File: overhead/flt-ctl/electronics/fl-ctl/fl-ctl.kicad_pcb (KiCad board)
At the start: 2 copper layers, 145 x 47.3 mm, 31 parts, among them J1 Conn_02x01, J2 Conn_02x05_Counter_Clockwise

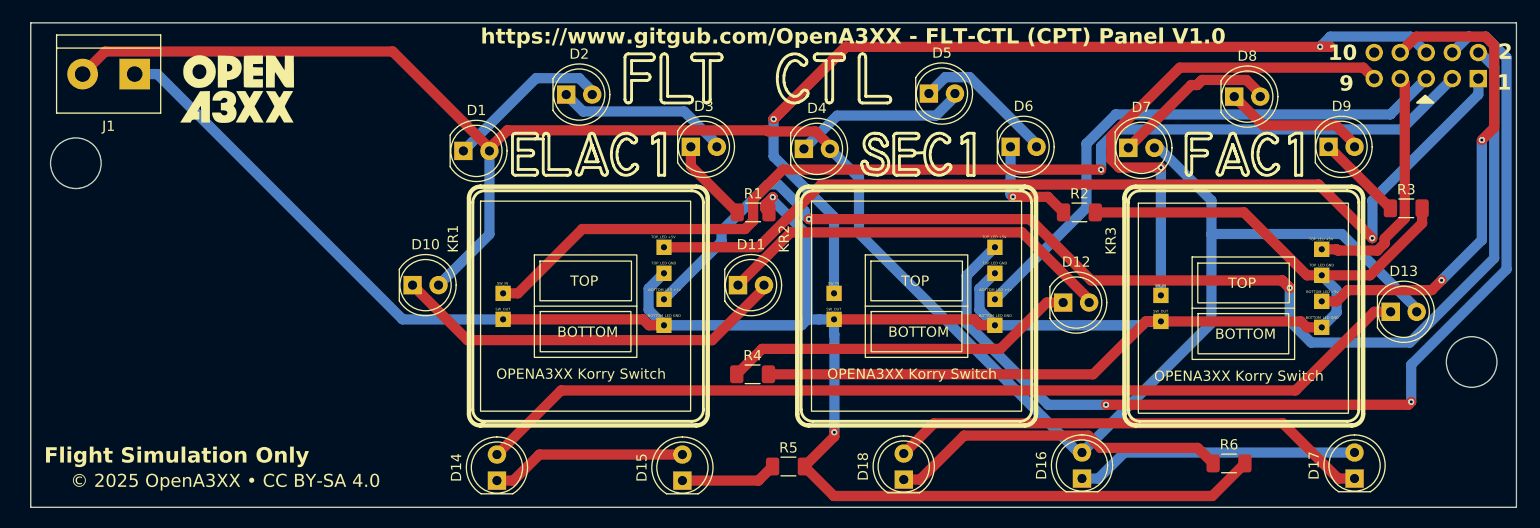
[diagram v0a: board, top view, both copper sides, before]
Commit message: Updated all LEDs for SMD!
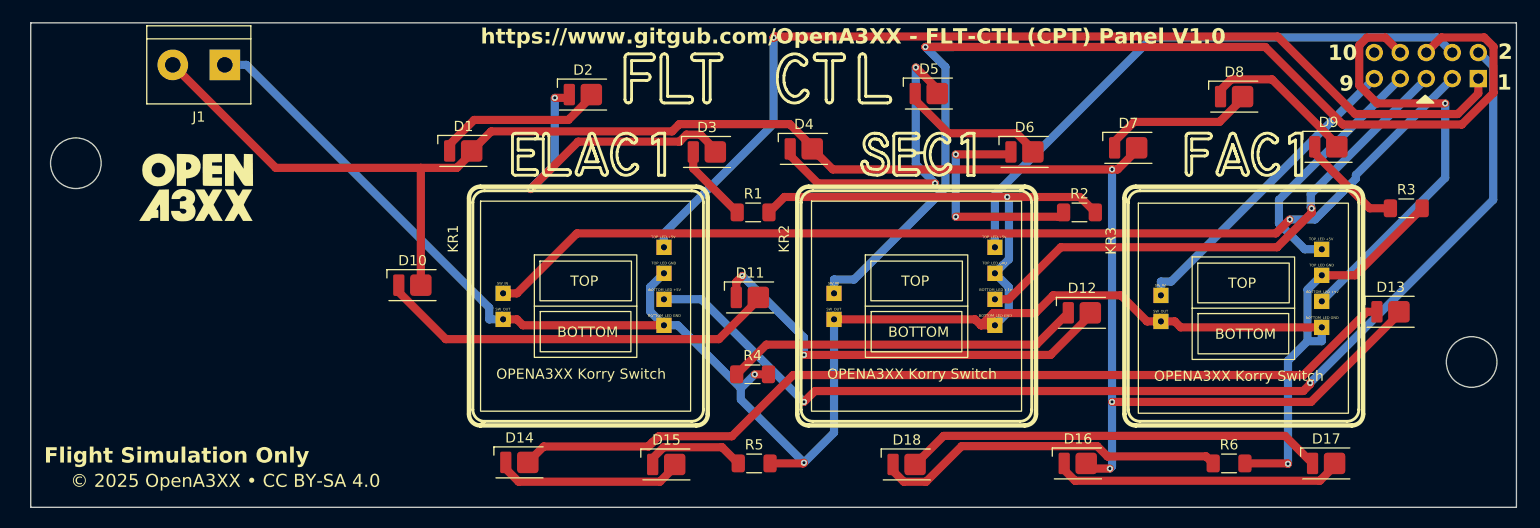
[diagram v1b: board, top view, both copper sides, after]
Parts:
- D1, D10, D11, D12, D13, D14, D15, D16, D17, D18, D2, D3, D4, D5, D6, D7, D8, D9: footprint LED_THT:LED_D5.0mm_Clear -> OpenA3XX:LED_Everlight-SMD3528_3.5x2.8mm_67-21ST
- moved LogoBottom 10.4 mm to (90.9, 92.9)
- moved LogoTop 10.4 mm to (90.9, 92.9)
- moved J1 8.85 mm to (93.6, 81.0)
- moved R5 3.36 mm to (145.3, 119.9)
- moved D17 3.13 mm to (201.1, 119.9), turned to 0 degrees
- moved D14 2.83 mm to (122.4, 119.8), turned to 0 degrees
- moved D15 2.22 mm to (136.7, 120.0), turned to 0 degrees
- moved D12 2.09 mm to (177.3, 105.2)
- moved D11 1.68 mm to (144.9, 103.7)
- moved D3 1.65 mm to (140.7, 89.5)
- moved D2 1.64 mm to (128.6, 83.9)
- moved D16 1.53 mm to (176.9, 119.9), turned to 0 degrees
- moved D18 1.51 mm to (160.2, 120.0), turned to 0 degrees
- moved D6 1.46 mm to (171.7, 89.5)
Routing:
- net GND: track 300.6 -> 240.2 mm, vias 2 -> 4
- net Net-(J2-Pin_4): track 99.6 -> 56.7 mm, vias 2 -> 0
- net Net-(J2-Pin_9): track 48.8 -> 30.4 mm, vias 1 -> 0
- net +12V: track 195.7 -> 178.1 mm, vias 0 -> 3
- net Net-(J2-Pin_6): track 131.0 -> 113.5 mm, vias 2 -> 1
- net Net-(D2-K): track 17.0 -> 32.5 mm, vias 0 -> 2
- net Net-(J2-Pin_2): track 123.2 -> 108.3 mm
- net Net-(D4-K): track 17.2 -> 31.4 mm, vias 0 -> 2
- net Net-(D6-K): track 10.5 -> 22.3 mm, vias 1 -> 2
- net Net-(D17-K): track 47.5 -> 41.1 mm
- net Net-(J2-Pin_1): track 93.7 -> 99.7 mm
- net Net-(J2-Pin_8): track 47.8 -> 42.3 mm, vias 2 -> 1
- net Net-(D13-K): track 93.0 -> 89.6 mm
- net Net-(D11-K): track 39.4 -> 42.3 mm, vias 0 -> 2
- net Net-(J2-Pin_5): track 54.7 -> 52.2 mm, vias 0 -> 1
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
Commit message: Added terminal connector to 3D models
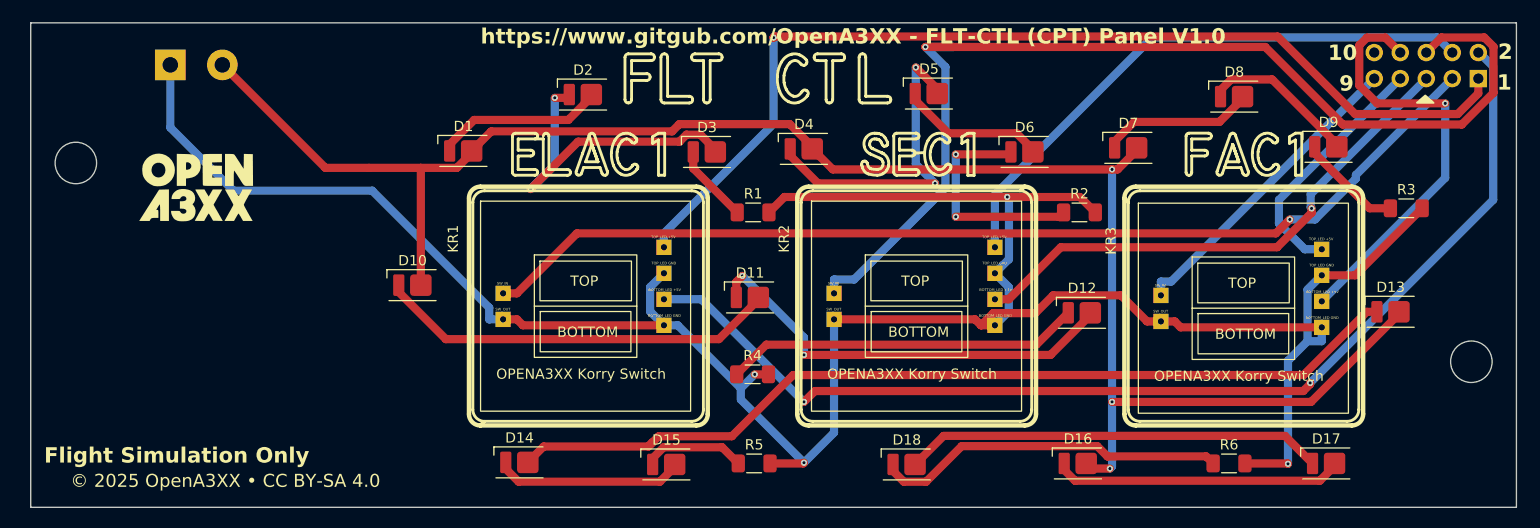
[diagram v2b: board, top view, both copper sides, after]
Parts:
- J1: moved to B.Cu
- moved J1 5.32 mm to (88.3, 81.0), turned to 0 degrees
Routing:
- net GND: track 240.2 -> 249.2 mm
- net +12V: track 178.1 -> 173.3 mm
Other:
- outline, holes or cut-outs redrawn
